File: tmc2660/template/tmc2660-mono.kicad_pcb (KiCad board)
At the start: 4 copper layers, 25 x 40 mm, 18 parts, among them J100 0R, M100 Mount, M101 Mount, P100 Motor, U100 TMC2660

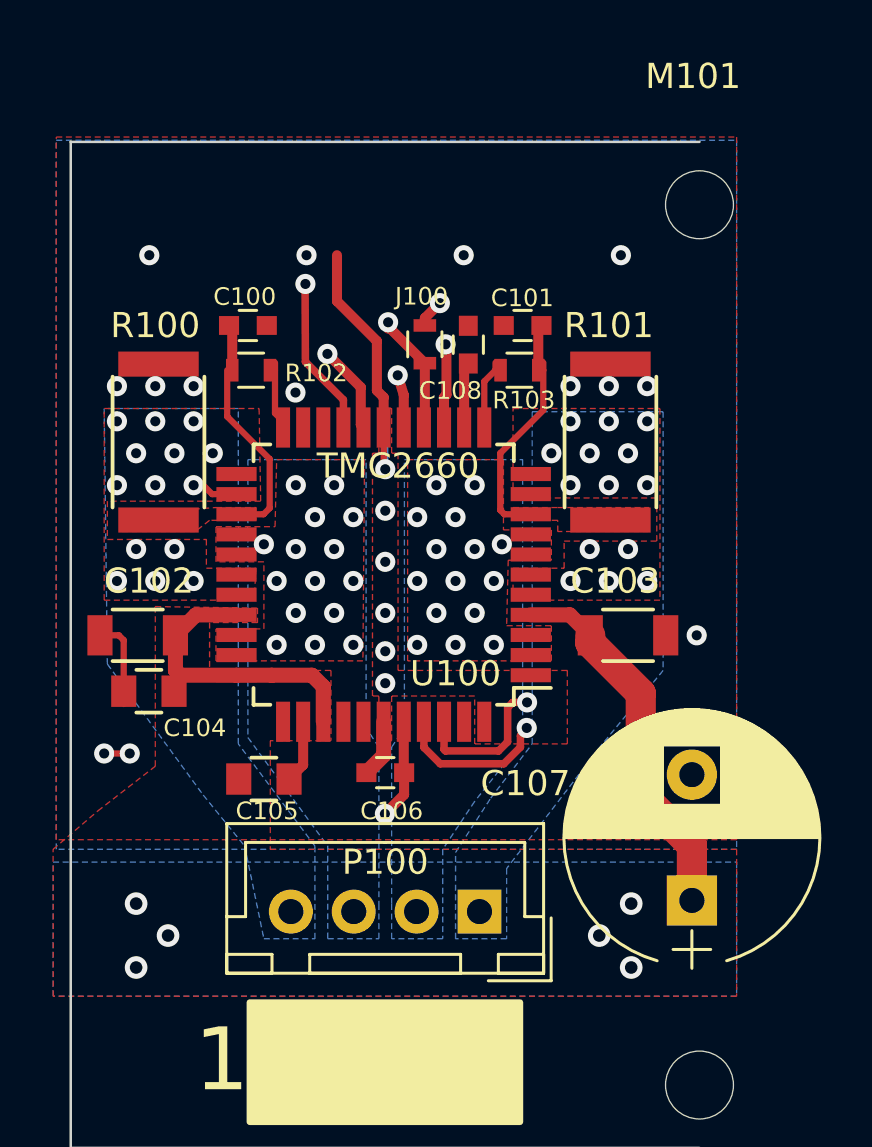
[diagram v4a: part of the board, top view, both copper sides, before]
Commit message: More DFM: choose more common physical capacitor sizes.
o Capacitors in the 100-150uF and 35-50V range are typically 8mm dia.
o Choose all 100nF same size. Even for 50V, there are 0603 available.
o Properly connect the 10nF smoothing capacitor for shunt feedback
  voltage (was connected to GND on the wrong side).
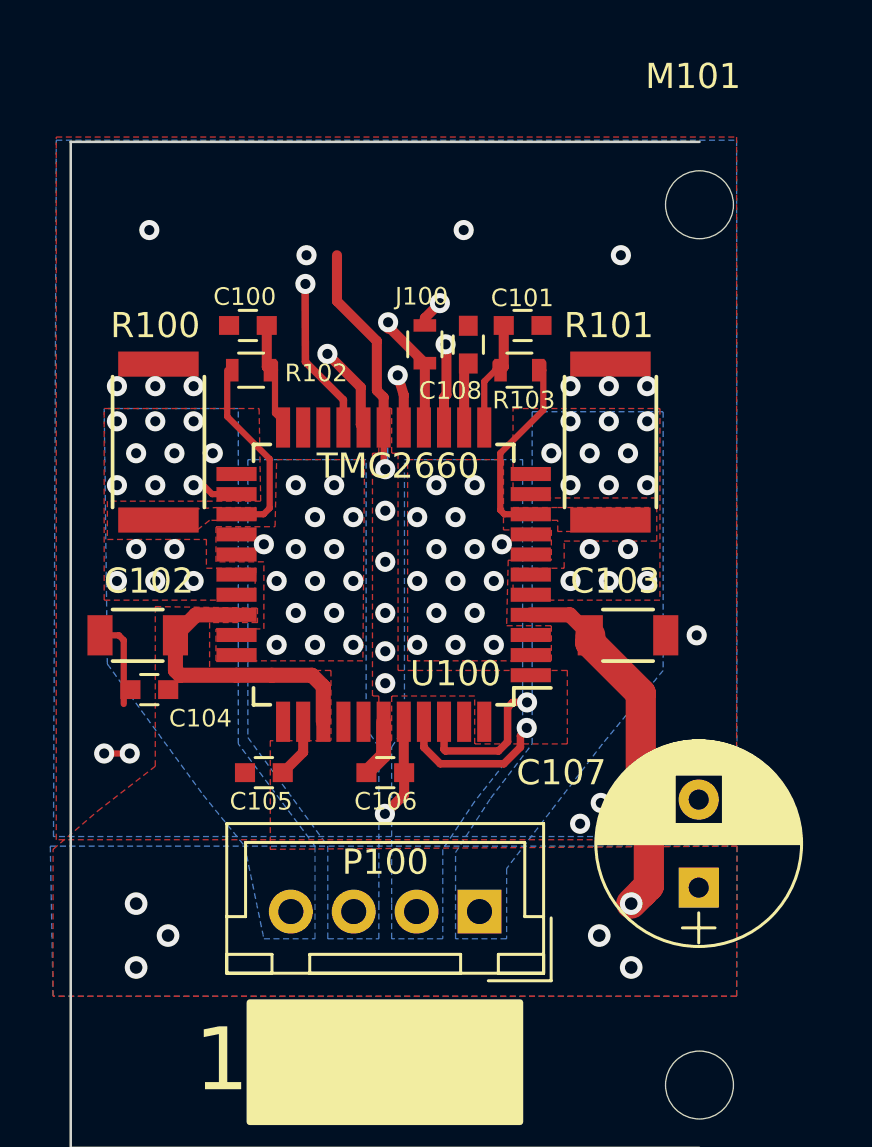
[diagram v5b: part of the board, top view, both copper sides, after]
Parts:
- C104, C105: footprint Capacitors_SMD:C_0805 -> Capacitors_SMD:C_0603
- C107: footprint Capacitors_THT:CP_Radial_D10.0mm_P5.00mm -> Capacitors_THT:CP_Radial_D8.0mm_P3.50mm
- moved C107 0.58 mm to (125.0, 89.7)
- moved C105 0.25 mm to (107.7, 85.1)
- moved C104 0.07 mm to (103.1, 81.8)
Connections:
- net Net-(C105-Pad2) renamed /TMC2660-100/VHS
- C100 pad 1: /TMC2660-100/BRB -> GND
- C100 pad 2: GND -> Net-(C100-Pad2)
- C101 pad 1: GND -> Net-(C101-Pad1)
- C101 pad 2: /TMC2660-100/BRA -> GND
- R102 pad 2: Net-(R102-Pad2) -> Net-(C100-Pad2)
- R103 pad 1: Net-(R103-Pad1) -> Net-(C101-Pad1)
- U100 pad 12: Net-(R103-Pad1) -> Net-(C101-Pad1)
- U100 pad 22: Net-(R102-Pad2) -> Net-(C100-Pad2)
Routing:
- net Net-(C101-Pad1): track 0.00 -> 4.59 mm
- net Net-(C100-Pad2): track 0.00 -> 4.54 mm
- net Net-(R103-Pad1): track 2.76 -> 0.00 mm
- net Net-(R102-Pad2): track 2.71 -> 0.00 mm
- net /TMC2660-100/BRA: track 10.2 -> 8.42 mm
- net /TMC2660-100/BRB: track 9.43 -> 7.60 mm
- net GND: track 17.4 -> 17.8 mm, vias 23 -> 22
